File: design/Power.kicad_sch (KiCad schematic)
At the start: 46 parts, among them J3 Screw_Terminal_01x02, J4 Screw_Terminal_01x03, Q1 IRF7854, Q2 IRF7854, Q3 IRF7854, Q4 IRF7854, Q5 IRF7854, Q6 IRF7854, U5 AD8418, U6 AD8418, U7 AD8418

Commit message: Agregue LCSC Part #
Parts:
- Q1, Q2, Q3, Q4, Q5, Q6: LCSC (none) -> C158109
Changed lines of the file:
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@@
+			)
+		)
+		(property "LCSC" "C158109"
+			(at 55.88 44.45 0)
+			(effects
+				(font
+					(size 1.27 1.27)
+				)
+				(hide yes)
 			)
 		)
@@
 			)
 		)
+		(property "LCSC" "C158109"
+			(at 55.88 77.47 0)
+			(effects
+				(font
+					(size 1.27 1.27)
+				)
+				(hide yes)
+			)
+		)
 		(pin "2"
 		)
@@
 			)
 		)
+		(property "LCSC" "C158109"
+			(at 149.86 44.45 0)
+			(effects
+				(font
+					(size 1.27 1.27)
+				)
+				(hide yes)
+			)
+		)
 		(pin "2"
 		)
@@
 			)
 		)
+		(property "LCSC" "C158109"
+			(at 149.86 77.47 0)
+			(effects
+				(font
+					(size 1.27 1.27)
+				)
+				(hide yes)
+			)
+		)
 		(pin "1"
 		)
@@
 			)
 		)
+		(property "LCSC" "C158109"
+			(at 238.76 74.93 0)
+			(effects
+				(font
+					(size 1.27 1.27)
+				)
+				(hide yes)
+			)
+		)
 		(pin "2"
 		)
@@
 			(at 238.76 44.45 0)
 			(effects
+				(font
+					(size 1.27 1.27)
+				)
+				(hide yes)
+			)
+		)
+		(property "LCSC" "C158109"
+			(at 238.76 44.45 0)
+			(effects

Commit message: Agregue LCSC Part # a algunas resistencias
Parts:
- R28: LCSC (none) -> C98220
- R29: LCSC (none) -> C163424
- R30: LCSC (none) -> C227479
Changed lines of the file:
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@@
+			)
+		)
+		(property "LCSC" "C98220"
+			(at 158.75 143.51 0)
+			(effects
+				(font
+					(size 1.27 1.27)
+				)
+				(hide yes)
 			)
 		)
@@
 			)
 		)
+		(property "LCSC" "C227479"
+			(at 208.28 151.13 0)
+			(effects
+				(font
+					(size 1.27 1.27)
+				)
+				(hide yes)
+			)
+		)
 		(pin "2"
 		)
@@
 			(at 208.28 130.81 0)
 			(effects
+				(font
+					(size 1.27 1.27)
+				)
+				(hide yes)
+			)
+		)
+		(property "LCSC" "C163424"
+			(at 208.28 130.81 0)
+			(effects

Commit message: Correccion de algunos DRC
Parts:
- R18, R24, R31: LCSC (none) -> C3033267; MPN CSNL2512FTL500 -> PA2512FKM7T0U5E; Manufacturer Stackpole Electronics Inc -> YAGEO
- R19, R20, R25, R26, R32, R33: LCSC (none) -> C137705
- R21, R22, R23: LCSC (none) -> C105588
- R27: LCSC (none) -> C524451
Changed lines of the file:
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@@
+			)
+		)
+		(property "LCSC" "C137705"
+			(at 153.67 45.72 0)
+			(effects
+				(font
+					(size 1.27 1.27)
+				)
+				(hide yes)
 			)
 		)
@@
 			)
 		)
-		(property "Manufacturer" "Stackpole Electronics Inc"
+		(property "Manufacturer" "YAGEO"
 			(at 129.54 55.88 0)
 			(effects
@@
 			)
 		)
-		(property "MPN" "CSNL2512FTL500"
+		(property "MPN" "PA2512FKM7T0U5E"
+			(at 129.54 55.88 0)
+			(effects
+				(font
+					(size 1.27 1.27)
+				)
+				(hide yes)
+			)
+		)
+		(property "LCSC" "C3033267"
 			(at 129.54 55.88 0)
 			(effects
@@
 		)
 		(property "MPN" "RC0603FR-074R7L"
+			(at 156.21 78.74 0)
+			(effects
+				(font
+					(size 1.27 1.27)
+				)
+				(hide yes)
+			)
+		)
+		(property "LCSC" "C137705"
 			(at 156.21 78.74 0)
 			(effects
@@
 			)
 		)
+		(property "LCSC" "C137705"
+			(at 57.15 45.72 0)
+			(effects
+				(font
+					(size 1.27 1.27)
+				)
+				(hide yes)
+			)
+		)
 		(pin "1"
 		)
@@
 			)
 		)
-		(property "Manufacturer" "Stackpole Electronics Inc"
+		(property "Manufacturer" "YAGEO"
 			(at 35.56 52.07 0)
 			(effects
@@
 			)
 		)
-		(property "MPN" "CSNL2512FTL500"
+		(property "MPN" "PA2512FKM7T0U5E"
+			(at 35.56 52.07 0)
+			(effects
+				(font
+					(size 1.27 1.27)
+				)
+				(hide yes)
+			)
+		)
+		(property "LCSC" "C3033267"
 			(at 35.56 52.07 0)
 			(effects
@@
 		)
 		(property "MPN" "RC0603FR-074R7L"
+			(at 59.69 78.74 0)
+			(effects
+				(font
+					(size 1.27 1.27)
+				)
+				(hide yes)
+			)
+		)
+		(property "LCSC" "C137705"
 			(at 59.69 78.74 0)
 			(effects
@@
 			)
 		)
+		(property "LCSC" "C137705"
+			(at 242.57 45.72 0)
+			(effects
+				(font
+					(size 1.27 1.27)
+				)
+				(hide yes)
+			)
+		)
 		(pin "1"
 		)
@@
 			)
 		)
-		(property "Manufacturer" "Stackpole Electronics Inc"
+		(property "Manufacturer" "YAGEO"
 			(at 218.44 55.88 0)
 			(effects
@@
 			)
 		)
-		(property "MPN" "CSNL2512FTL500"
+		(property "MPN" "PA2512FKM7T0U5E"
+			(at 218.44 55.88 0)
+			(effects
+				(font
+					(size 1.27 1.27)
+				)
+				(hide yes)
+			)
+		)
+		(property "LCSC" "C3033267"
 			(at 218.44 55.88 0)
 			(effects
@@
 			)
 		)
+		(property "LCSC" "C137705"
+			(at 245.11 76.2 0)
+			(effects
+				(font
+					(size 1.27 1.27)
+				)
+				(hide yes)
+			)
+		)
 		(pin "2"
 		)
@@
 			)
 		)
+		(property "LCSC" "C105588"
+			(at 128.27 140.97 0)
+			(effects
+				(font
+					(size 1.27 1.27)
+				)
+				(hide yes)
+			)
+		)
 		(pin "2"
 		)
@@
 			)
 		)
+		(property "LCSC" "C105588"
+			(at 128.27 161.29 0)
+			(effects
+				(font
+					(size 1.27 1.27)
+				)
+				(hide yes)
+			)
+		)
 		(pin "1"
 		)
@@
 		)
 		(property "MPN" "RC0603FR-07100RL"
+			(at 128.27 179.07 0)
+			(effects
+				(font
+					(size 1.27 1.27)
+				)
+				(hide yes)
+			)
+		)
+		(property "LCSC" "C105588"
 			(at 128.27 179.07 0)
 			(effects
@@
 			(at 158.75 133.35 0)
 			(effects
+				(font
+					(size 1.27 1.27)
+				)
+				(hide yes)
+			)
+		)
+		(property "LCSC" "C524451"
+			(at 158.75 133.35 0)
+			(effects

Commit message: Correccion de DRC
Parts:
- U5, U6, U7: LCSC (none) -> C462197
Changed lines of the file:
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@@
+			)
+		)
+		(property "LCSC" "C462197"
+			(at 35.56 73.66 0)
+			(effects
+				(font
+					(size 1.27 1.27)
+				)
+				(hide yes)
 			)
 		)
@@
 			)
 		)
+		(property "LCSC" "C462197"
+			(at 218.44 73.66 0)
+			(effects
+				(font
+					(size 1.27 1.27)
+				)
+				(hide yes)
+			)
+		)
 		(pin "4"
 		)
@@
 			(at 129.54 73.66 0)
 			(effects
+				(font
+					(size 1.27 1.27)
+				)
+				(hide yes)
+			)
+		)
+		(property "LCSC" "C462197"
+			(at 129.54 73.66 0)
+			(effects

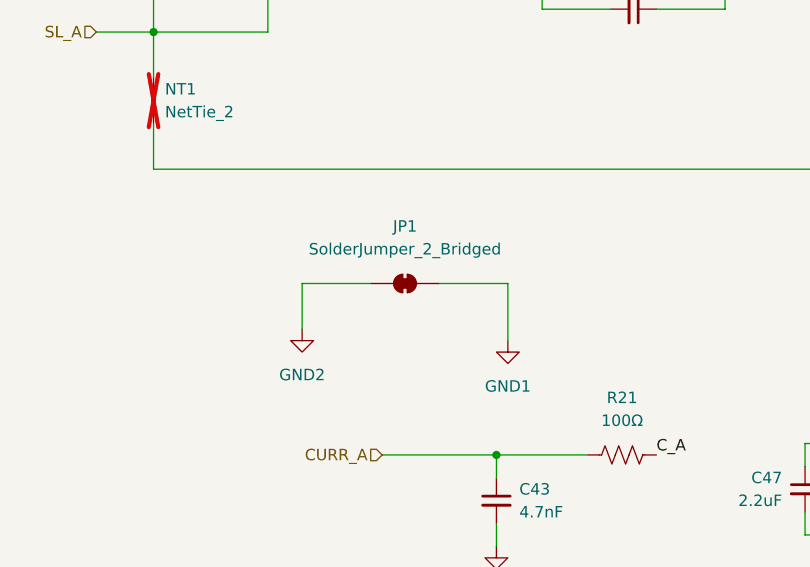
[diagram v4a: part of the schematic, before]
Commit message: Cambio de switch de tension del sensor por jumper
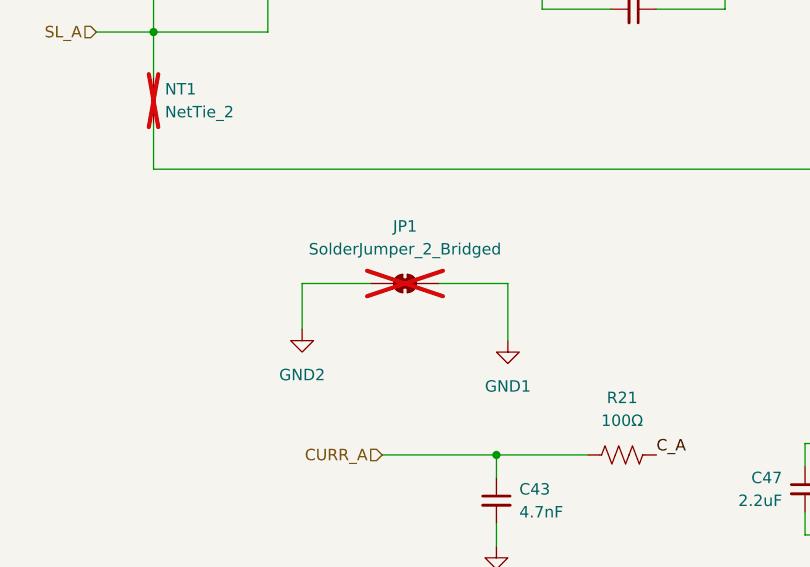
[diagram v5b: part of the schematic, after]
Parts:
- JP1: now not fitted
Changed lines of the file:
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@@
 		(in_bom no)
 		(on_board yes)
-		(dnp no)
+		(dnp yes)
 		(fields_autoplaced yes)
 		(property "Reference" "JP1"

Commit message: Abaratando costos
Cambios en numeros de jlcpcb, pasados a componentes básicos
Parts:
- J3, J4, TP1, TP2, TP3: now left out of the parts list
- R19, R20, R25, R26, R32, R33: LCSC C137705 -> C23164
- R21, R22, R23: LCSC C105588 -> C22775
- R28: LCSC C98220 -> C25804
- R29: LCSC C163424 -> C23153
- R30: LCSC C227479 -> C4190
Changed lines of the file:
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@@
 			)
 		)
-		(property "LCSC" "C137705"
+		(property "LCSC" "C23164"
 			(at 153.67 45.72 0)
 			(effects
@@
 			)
 		)
-		(property "LCSC" "C137705"
+		(property "LCSC" "C23164"
 			(at 156.21 78.74 0)
 			(effects
@@
 			)
 		)
-		(property "LCSC" "C137705"
+		(property "LCSC" "C23164"
 			(at 57.15 45.72 0)
 			(effects
@@
 			)
 		)
-		(property "LCSC" "C137705"
+		(property "LCSC" "C23164"
 			(at 59.69 78.74 0)
 			(effects
@@
 			)
 		)
-		(property "LCSC" "C137705"
+		(property "LCSC" "C23164"
 			(at 242.57 45.72 0)
 			(effects
@@
 			)
 		)
-		(property "LCSC" "C137705"
+		(property "LCSC" "C23164"
 			(at 245.11 76.2 0)
 			(effects
@@
 			)
 		)
-		(property "LCSC" "C105588"
+		(property "LCSC" "C22775"
 			(at 128.27 140.97 0)
 			(effects
@@
 			)
 		)
-		(property "LCSC" "C105588"
+		(property "LCSC" "C22775"
 			(at 128.27 161.29 0)
 			(effects
@@
 			)
 		)
-		(property "LCSC" "C105588"
+		(property "LCSC" "C22775"
 			(at 128.27 179.07 0)
 			(effects
@@
 			)
 		)
-		(property "LCSC" "C98220"
+		(property "LCSC" "C25804"
 			(at 158.75 143.51 0)
 			(effects
@@
 			)
 		)
-		(property "LCSC" "C227479"
+		(property "LCSC" "C4190"
 			(at 208.28 151.13 0)
 			(effects
@@
 		(unit 1)
 		(exclude_from_sim no)
-		(in_bom yes)
+		(in_bom no)
 		(on_board yes)
 		(dnp yes)
@@
 		(unit 1)
 		(exclude_from_sim no)
-		(in_bom yes)
+		(in_bom no)
 		(on_board yes)
 		(dnp yes)
@@
 		(unit 1)
 		(exclude_from_sim no)
-		(in_bom yes)
+		(in_bom no)
 		(on_board yes)
 		(dnp yes)
@@
 		(unit 1)
 		(exclude_from_sim no)
-		(in_bom yes)
+		(in_bom no)
 		(on_board yes)
 		(dnp no)
@@
 			)
 		)
-		(property "LCSC" "C163424"
+		(property "LCSC" "C23153"
 			(at 208.28 130.81 0)
 			(effects
@@
 		(unit 1)
 		(exclude_from_sim no)
-		(in_bom yes)
+		(in_bom no)
 		(on_board yes)
 		(dnp no)

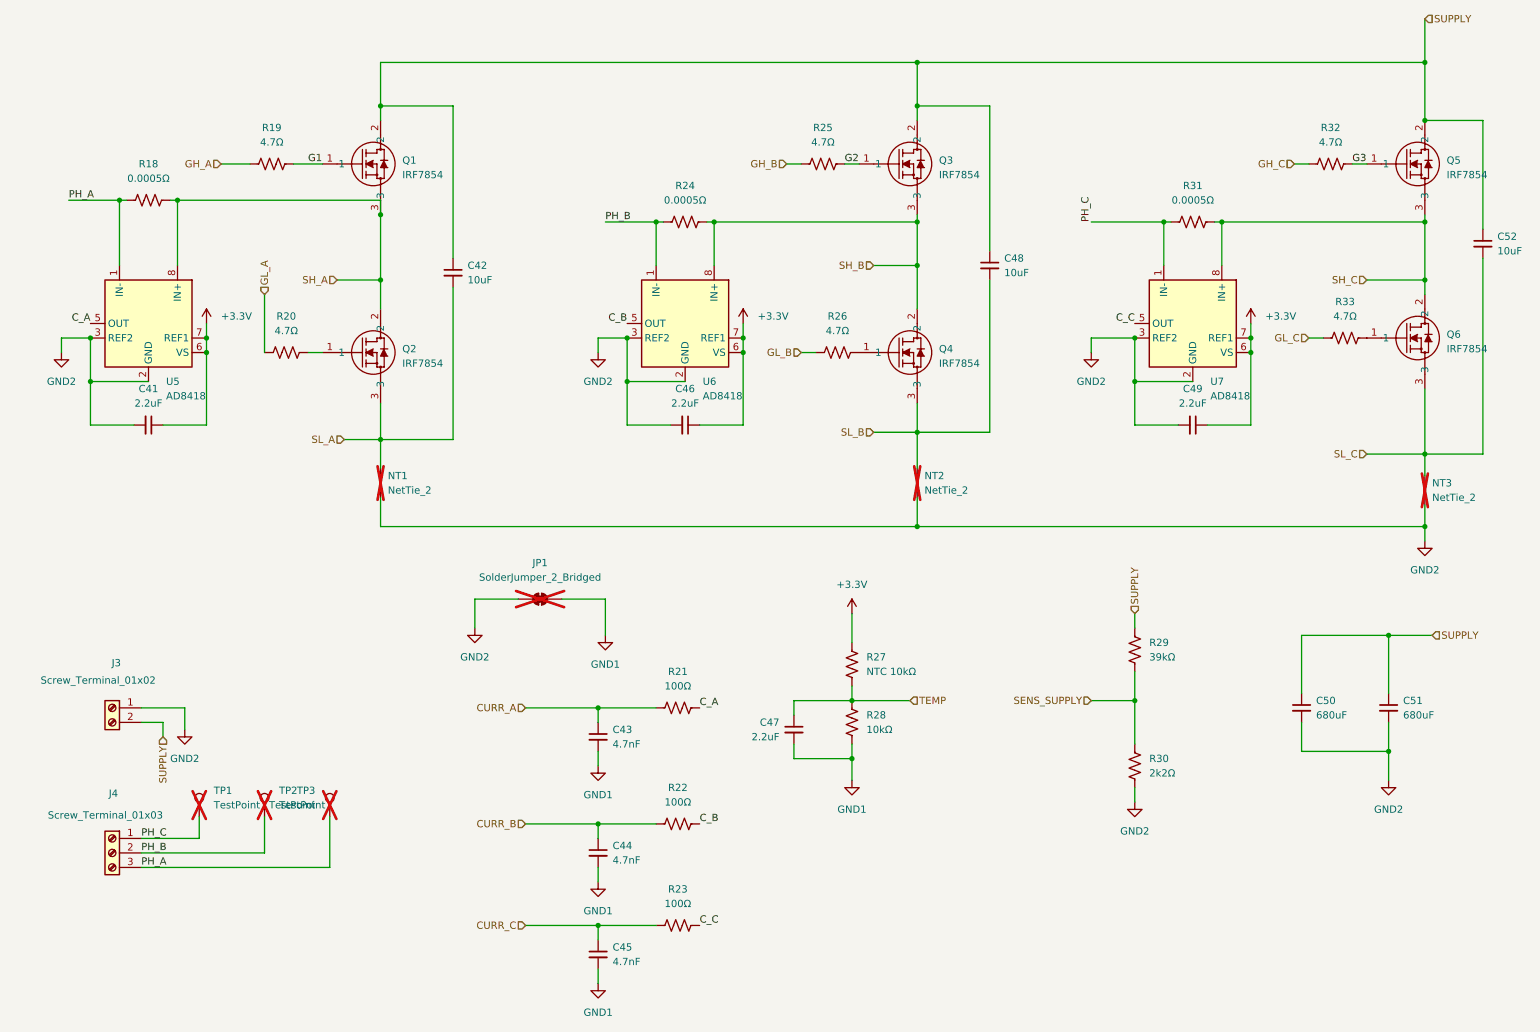
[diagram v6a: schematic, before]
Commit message: Pequeños cambios finales
Agregado de test points, cambiado de algunos footprints, agregado de QR
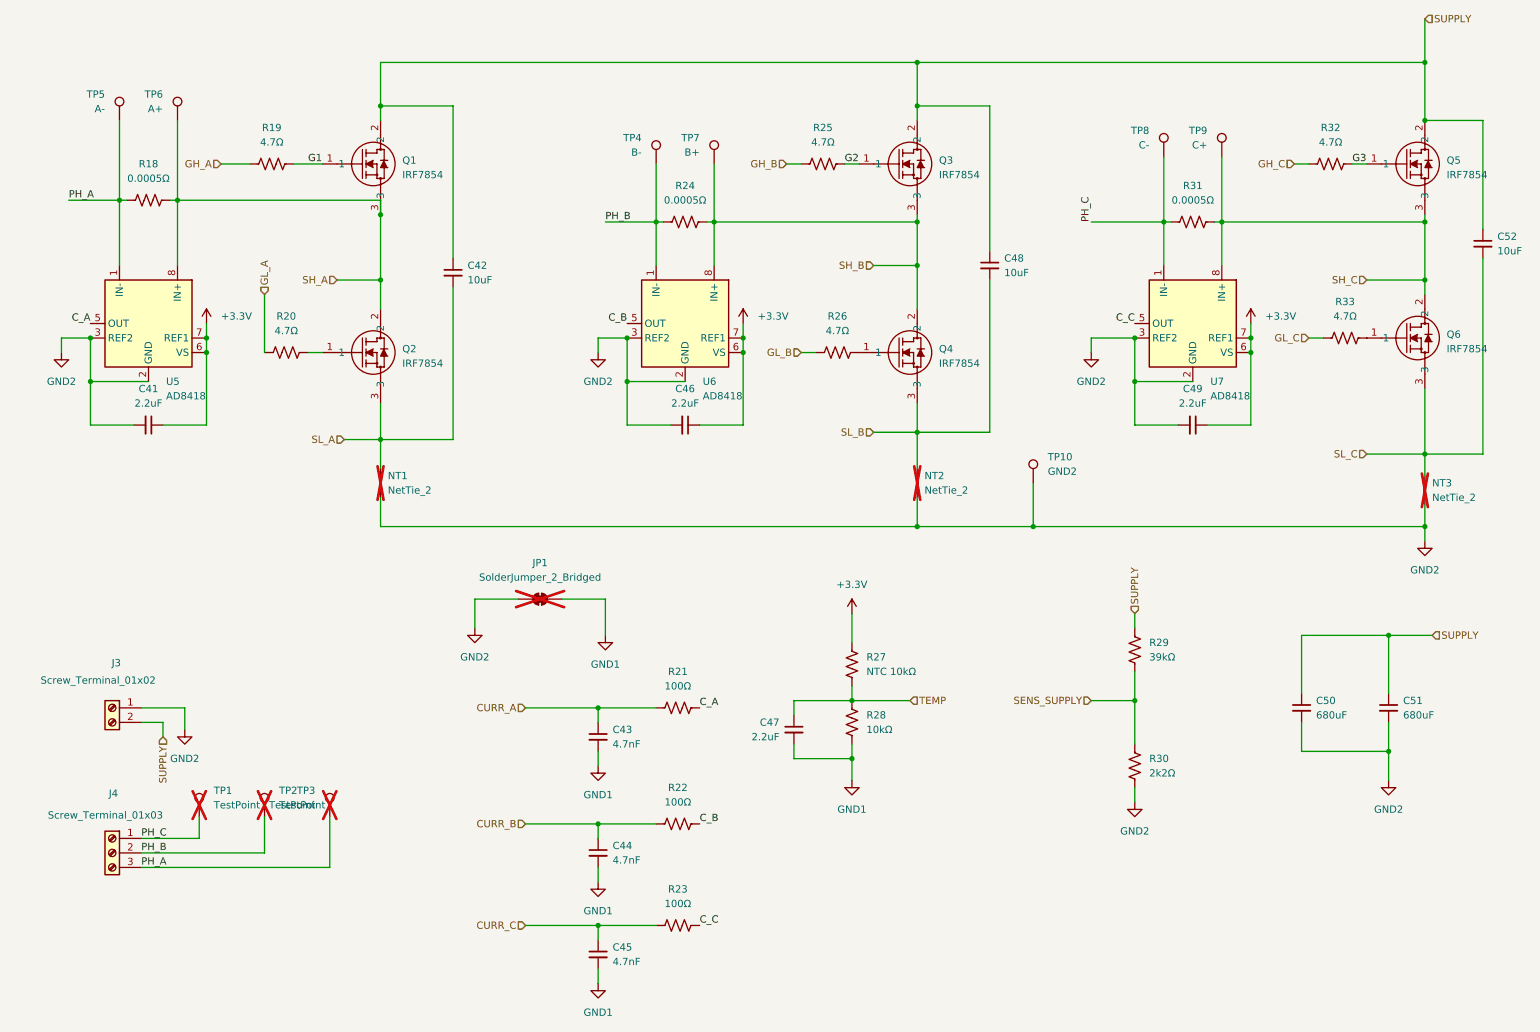
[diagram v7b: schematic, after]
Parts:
- added TP10: GND2, Connector_PinHeader_2.54mm:PinHeader_1x01_P2.54mm_Vertical, symbol Connector:TestPoint
- added TP4: B-, Connector_PinHeader_2.54mm:PinHeader_1x01_P2.54mm_Vertical, symbol Connector:TestPoint
- added TP5: A-, Connector_PinHeader_2.54mm:PinHeader_1x01_P2.54mm_Vertical, symbol Connector:TestPoint
- added TP6: A+, Connector_PinHeader_2.54mm:PinHeader_1x01_P2.54mm_Vertical, symbol Connector:TestPoint
- added TP7: B+, Connector_PinHeader_2.54mm:PinHeader_1x01_P2.54mm_Vertical, symbol Connector:TestPoint
- added TP8: C-, Connector_PinHeader_2.54mm:PinHeader_1x01_P2.54mm_Vertical, symbol Connector:TestPoint
- added TP9: C+, Connector_PinHeader_2.54mm:PinHeader_1x01_P2.54mm_Vertical, symbol Connector:TestPoint
- Q1, Q2, Q3, Q4, Q5, Q6: footprint crf1:SO-8_INF_IRF7854 -> crf1:SO-8_3.9x4.9mm_P1.27mm
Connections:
- net GND2: now also TP10.1
- net PH_A: now also TP5.1
- net PH_B: now also TP4.1
- net PH_C: now also TP8.1
- net SH_A: now also TP6.1
- net SH_B: now also TP7.1
- net SH_C: now also TP9.1

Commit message: cambios en la BOM
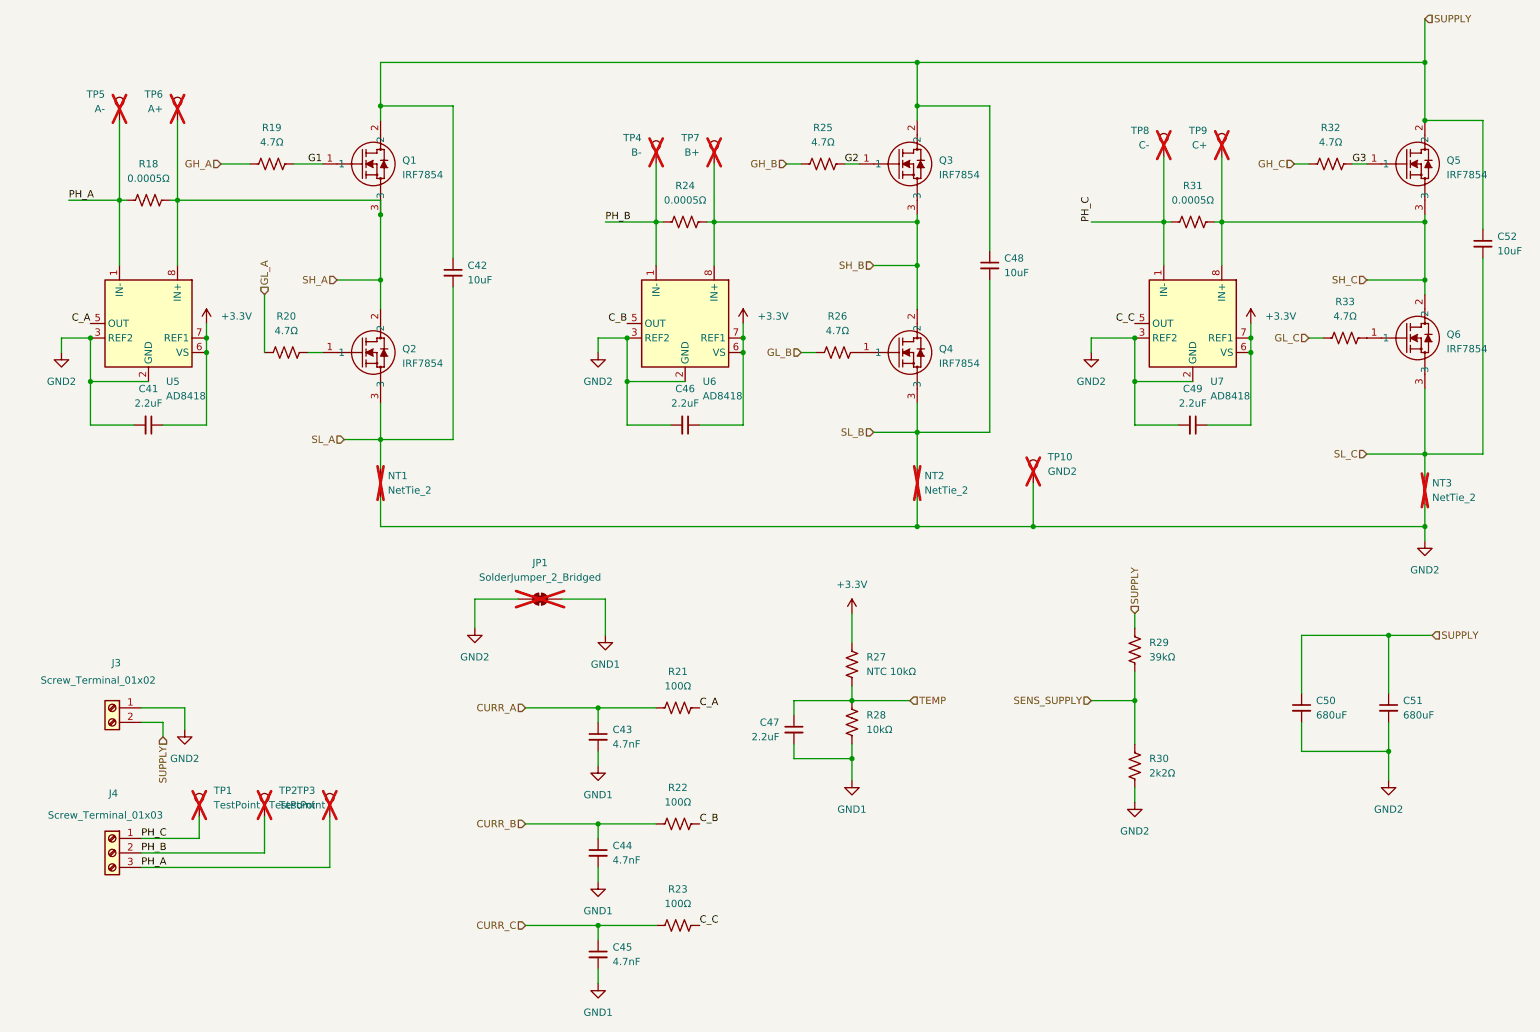
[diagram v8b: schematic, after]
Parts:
- TP10, TP4, TP5, TP6, TP7, TP8, TP9: now not fitted
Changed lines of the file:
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@@
 		(in_bom yes)
 		(on_board yes)
-		(dnp no)
+		(dnp yes)
 		(property "Reference" "TP6"
 			(at 38.1 33.5279 0)
@@
 		(in_bom yes)
 		(on_board yes)
-		(dnp no)
+		(dnp yes)
 		(property "Reference" "TP8"
 			(at 210.82 39.8779 0)
@@
 		(in_bom yes)
 		(on_board yes)
-		(dnp no)
+		(dnp yes)
 		(property "Reference" "TP9"
 			(at 220.98 39.8779 0)
@@
 		(in_bom yes)
 		(on_board yes)
-		(dnp no)
+		(dnp yes)
 		(property "Reference" "TP4"
 			(at 121.92 41.1479 0)
@@
 		(in_bom yes)
 		(on_board yes)
-		(dnp no)
+		(dnp yes)
 		(property "Reference" "TP7"
 			(at 132.08 41.1479 0)
@@
 		(in_bom yes)
 		(on_board yes)
-		(dnp no)
+		(dnp yes)
 		(property "Reference" "TP10"
 			(at 193.04 97.0279 0)
@@
 		(in_bom yes)
 		(on_board yes)
-		(dnp no)
+		(dnp yes)
 		(property "Reference" "TP5"
 			(at 27.94 33.5279 0)
